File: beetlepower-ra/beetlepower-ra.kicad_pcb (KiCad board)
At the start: 2 copper layers, 41 x 29 mm, 14 parts, among them J1 Battery, J2 OUT2, J3 OUT3, J4 OUT4, J5 Conn_01x03_Male, U1 MC7805

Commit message: Beetlepower right angle board
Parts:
- C1: footprint beetlepower-xt30:C-pth-and-smd -> Capacitor_SMD:C_0805_2012Metric_Pad1.18x1.45mm_HandSolder
- R1: footprint beetlepower-xt30:Resistor-pth-and-smd -> Resistor_SMD:R_0805_2012Metric_Pad1.20x1.40mm_HandSolder
- moved C1 18.6 mm to (84.5, 72.5)
- moved U1 1.83 mm to (85.5, 79.4)
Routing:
- net /GND: track 23.7 -> 15.1 mm, vias 1 -> 0
- net /B+: track 15.2 -> 17.6 mm
- net +5V: track 39.2 -> 41.1 mm
- net Net-(D1-Pad1): track 10.1 -> 8.36 mm
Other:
- board text removed: "Beetlepower RA"

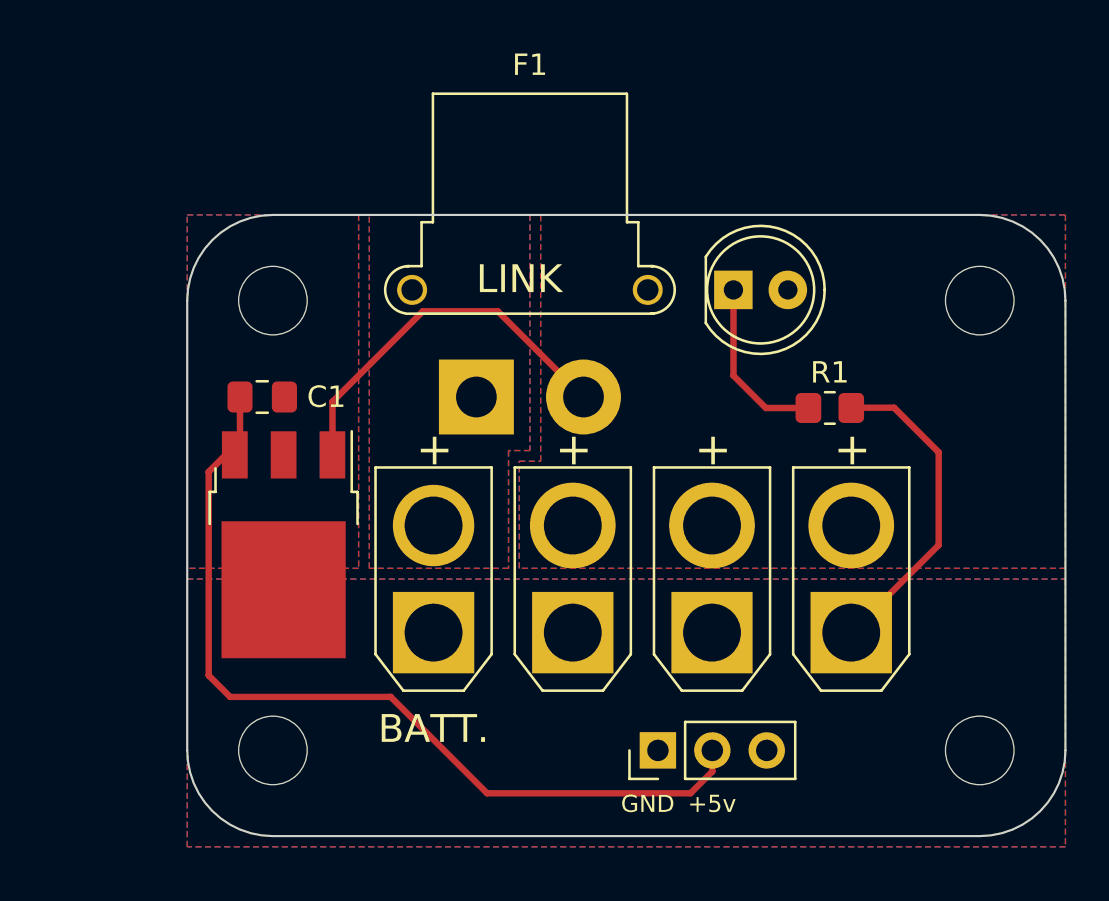
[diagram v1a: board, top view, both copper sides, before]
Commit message: Another version of Beetlepower RA with cable tie slots
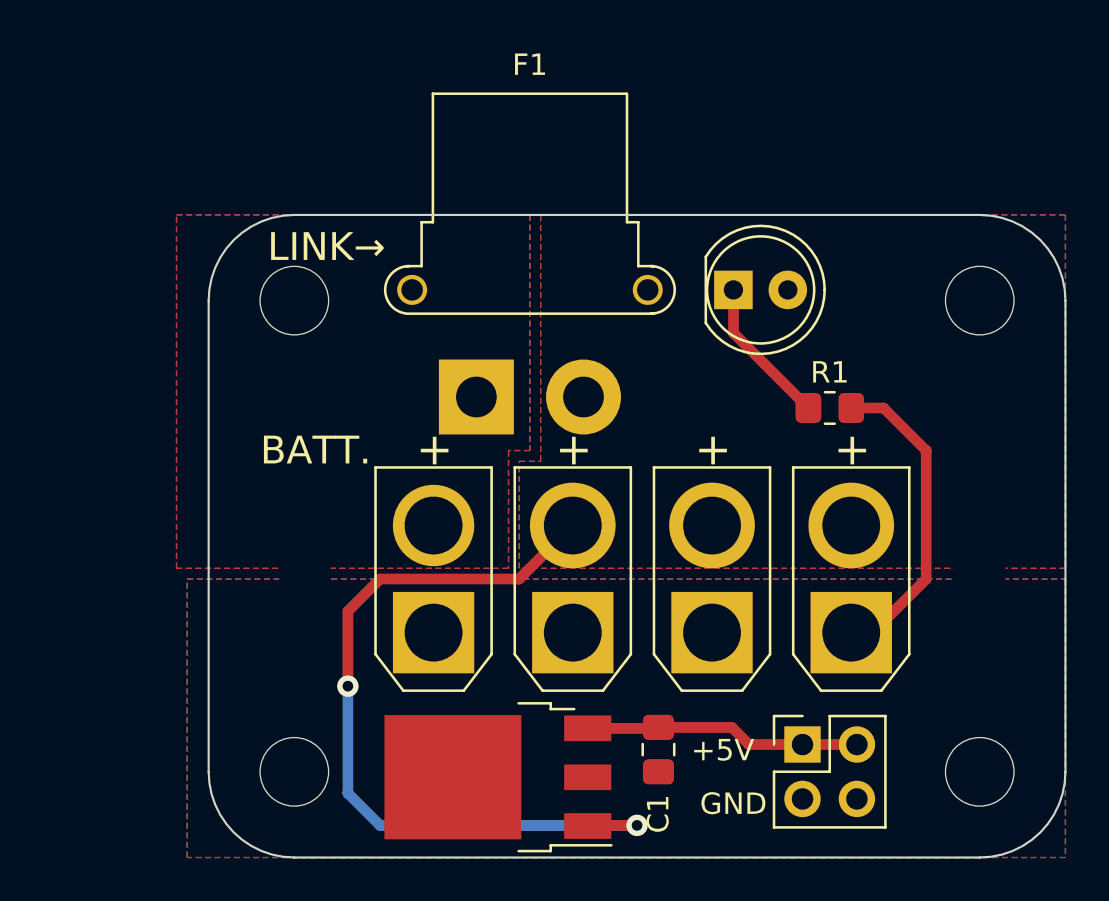
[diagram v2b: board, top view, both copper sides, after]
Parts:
- added H5: Slot, beetlepower-xt30:cabletie_slot, F.Cu at (118.0, 81.0)
- added H6: Slot, beetlepower-xt30:cabletie_slot, F.Cu at (86.5, 81.0)
- C1: value C -> 2.2uf
- J5: value Conn_01x03_Male -> becout; footprint Connector_PinHeader_2.54mm:PinHeader_1x03_P2.54mm_Vertical -> Connector_PinHeader_2.54mm:PinHeader_2x02_P2.54mm_Vertical
- R1: value R -> 1.5k
- moved C1 24.8 mm to (103.0, 89.0), turned to -90 degrees
- moved U1 14.8 mm to (95.5, 90.2), turned to 180 degrees
- moved J5 6.76 mm to (109.7, 88.7), turned to 0 degrees
- moved H2 1.41 mm to (86.0, 90.0)
- moved H1 1.00 mm to (86.0, 68.0)
- moved H4 1.00 mm to (118.0, 90.0)
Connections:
- J5 pad 1: /GND -> +5V
- J5 pad 3: unconnected-(J5-Pad3) -> /GND
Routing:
- net +5V: track 41.1 -> 12.9 mm
- net /B+: track 17.6 -> 37.1 mm, vias 0 -> 2
- net Net-(D1-Pad1): track 8.36 -> 6.96 mm
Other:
- board size 41 x 29 mm -> 40 x 30 mm
- board text added: "+5V"
- board text added: "LINK→"
- board text removed: "+5v"
